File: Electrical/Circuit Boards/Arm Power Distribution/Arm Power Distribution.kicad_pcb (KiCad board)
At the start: 2 copper layers, 61 x 58.4 mm, 12 parts, among them J1 XT60-F, J10 XT60-M, J12 XT60-F, J13 XT60-F, J2 XT60-F, J3 XT60-F, J4 XT60-F, J5 XT60-F, J6 XT60-F, J7 XT60-F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

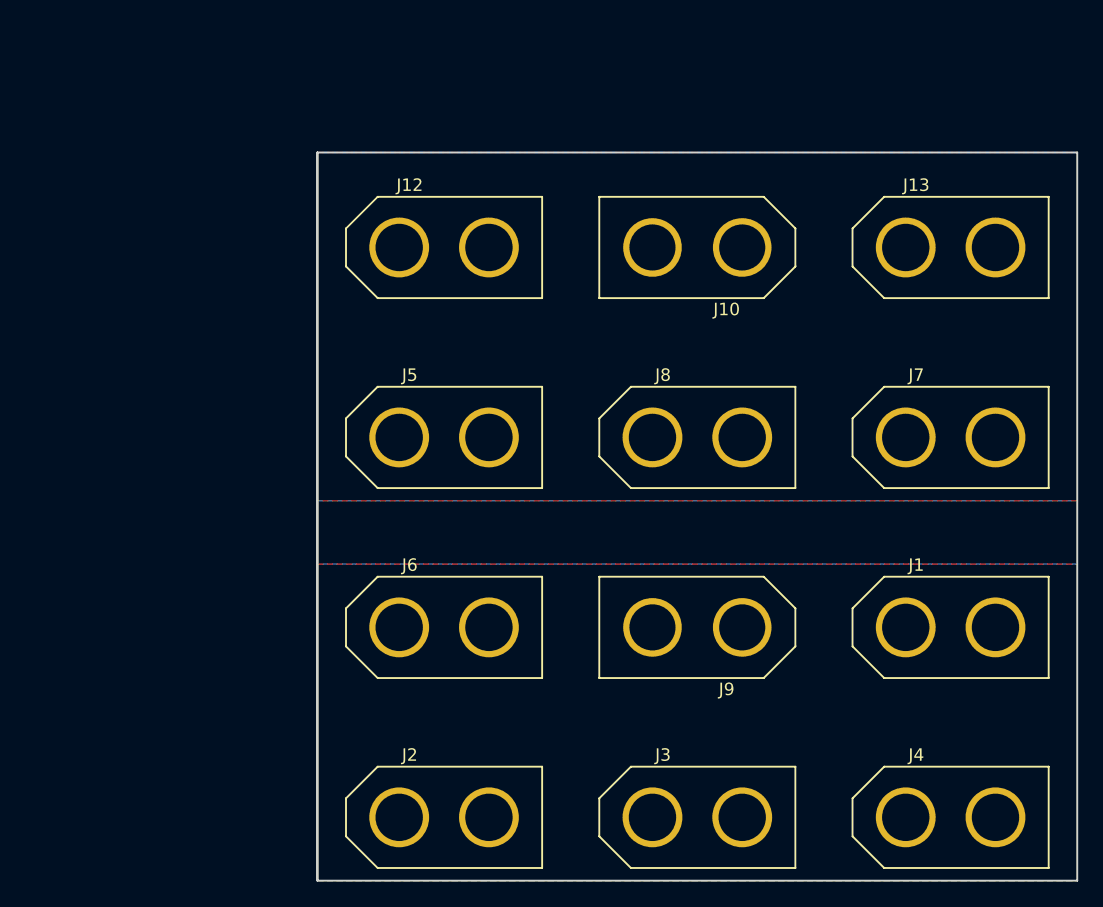
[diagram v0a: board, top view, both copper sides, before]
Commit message: Added an 8-channel ADC HAT (10 kHz chip)
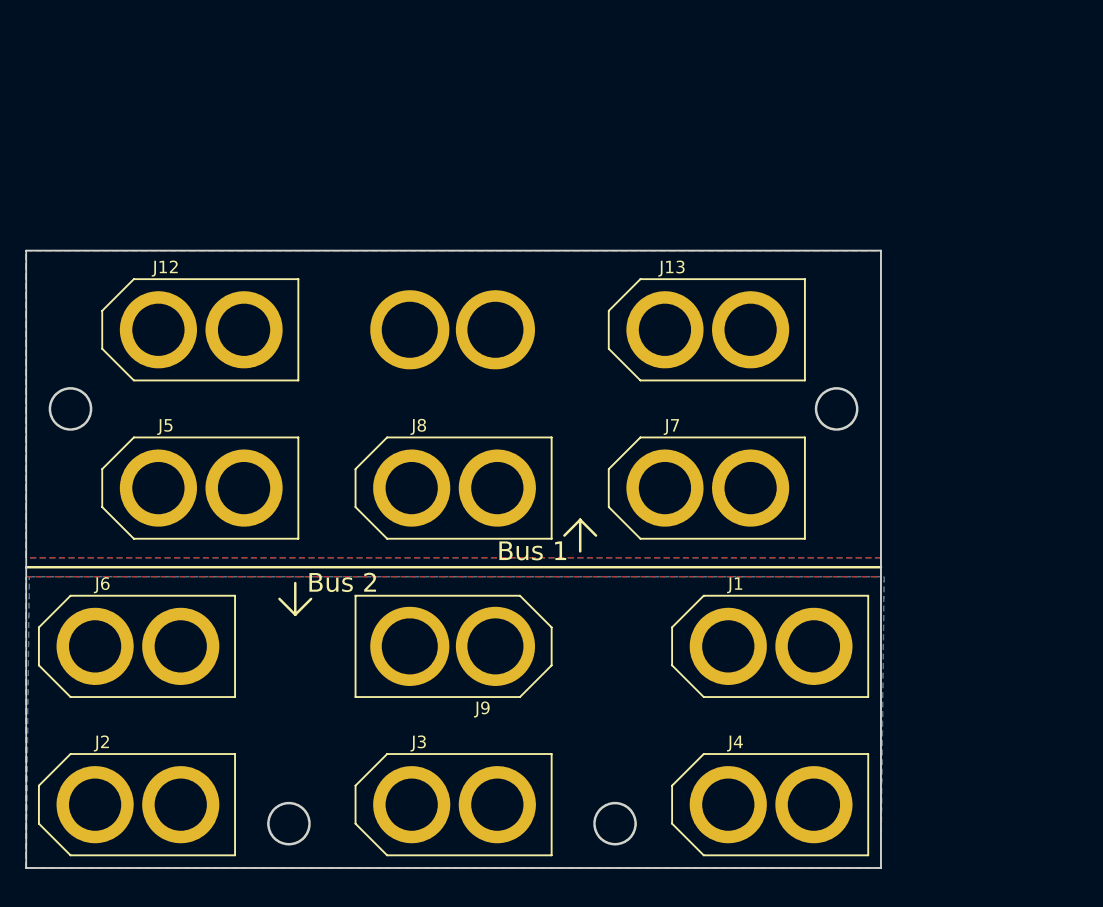
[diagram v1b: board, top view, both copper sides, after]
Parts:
- J10: moved to B.Cu
- moved J6 24.7 mm to (117.6, 113.3)
- moved J2 24.7 mm to (117.6, 126.0)
- moved J12 20.6 mm to (122.7, 87.9)
- moved J10 20.6 mm to (143.0, 87.9), turned to 90 degrees
- moved J13 20.6 mm to (163.3, 87.9)
- moved J5 20.0 mm to (122.7, 100.6)
- moved J7 20.0 mm to (163.3, 100.6)
- moved J8 20.0 mm to (143.0, 100.6)
- moved J9 19.6 mm to (143.0, 113.3)
- moved J3 19.6 mm to (143.0, 126.0)
- moved J1 14.6 mm to (168.4, 113.3)
- moved J4 14.5 mm to (168.4, 126.0)
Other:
- board size 61 x 58.4 mm -> 68.6 x 49.5 mm
- board text added: "Bus 1"
- board text added: "Bus 2"

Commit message: Arm Power Distribution Board (ordered)
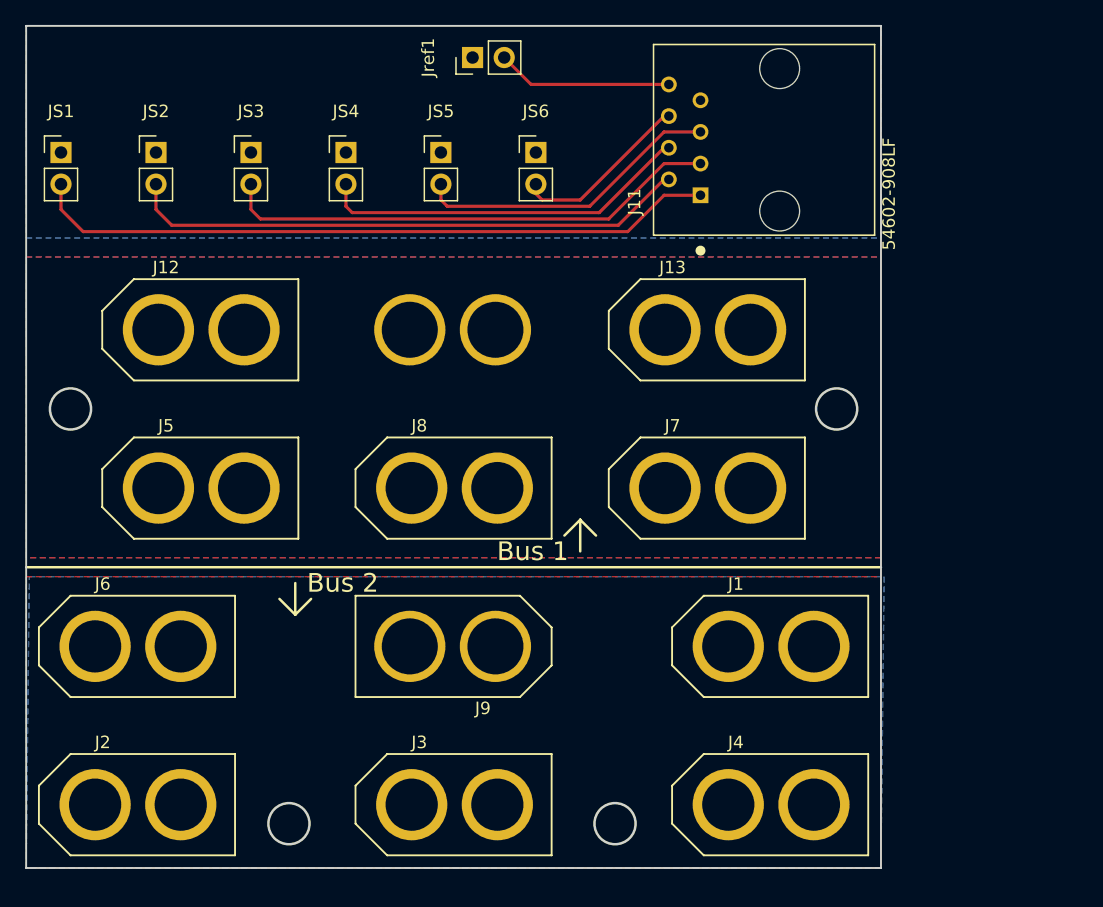
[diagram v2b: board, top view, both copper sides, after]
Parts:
- added J11: 54602-908LF, AMPHENOL_54602-908LF, F.Cu at (169.2, 72.6)
- added JS1: CONN_01X02_MALE, Pin_Headers:Pin_Header_Straight_1x02_Pitch2.54mm, F.Cu at (111.5, 73.7)
- added JS2: CONN_01X02_MALE, Pin_Headers:Pin_Header_Straight_1x02_Pitch2.54mm, F.Cu at (119.1, 73.7)
- added JS3: CONN_01X02_MALE, Pin_Headers:Pin_Header_Straight_1x02_Pitch2.54mm, F.Cu at (126.7, 73.7)
- added JS4: CONN_01X02_MALE, Pin_Headers:Pin_Header_Straight_1x02_Pitch2.54mm, F.Cu at (134.4, 73.7)
- added JS5: CONN_01X02_MALE, Pin_Headers:Pin_Header_Straight_1x02_Pitch2.54mm, F.Cu at (142.0, 73.7)
- added JS6: CONN_01X02_MALE, Pin_Headers:Pin_Header_Straight_1x02_Pitch2.54mm, F.Cu at (149.6, 73.7)
- added Jref1: CONN_01X02_MALE, Pin_Headers:Pin_Header_Straight_1x02_Pitch2.54mm, F.Cu at (144.5, 66.0)
- J1, J12, J13, J2, J3, J4, J5, J6, J7, J8: footprint Power Connectors:XT60-F -> Power_Connectors:XT60-F
- J10, J9: footprint Power Connectors:XT60-M -> Power_Connectors:XT60-M
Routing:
- net Net-(J11-Pad1): track 0.00 -> 55.3 mm
- net Net-(J11-Pad2): track 0.00 -> 45.2 mm
- net Net-(J11-Pad3): track 0.00 -> 40.3 mm
- net Net-(J11-Pad4): track 0.00 -> 29.8 mm
- net Net-(J11-Pad5): track 0.00 -> 24.8 mm
- net Net-(J11-Pad6): track 0.00 -> 14.5 mm
- net Net-(J11-Pad8): track 0.00 -> 14.2 mm
- added copper zone on B.Cu, net Net-(J11-Pad7)
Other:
- board size 68.6 x 49.5 mm -> 68.6 x 67.6 mm
